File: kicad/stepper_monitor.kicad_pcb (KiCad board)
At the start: 2 copper layers, 38.5 x 43 mm, 54 parts, among them J1 Conn_01x04_Male, J2 Conn_01x04_Male, J3 Conn_01x02_Male, J4 USB_C_Receptacle_USB2.0, J5 JTAG, Q1 UMH3N, Q2 PJA3439, SW1 SW_Push, U1 CP2102N-A01-GQFN28, U2 AMS1117-3.3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

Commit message: Change adc filter caps from 4.7n to 2.2n
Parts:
- C17, C18: value 4n7 -> 2n2
- C7: value 4u7 -> 2u2
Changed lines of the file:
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@@
     (descr "Capacitor SMD 0402 (1005 Metric), square (rectangular) end terminal, IPC_7351 nominal, (Body size source: IPC-SM-782 page 76, https://www.pcb-3d.com/wordpress/wp-content/uploads/ipc-sm-782a_amendment_1_and_2.pdf), generated with kicad-footprint-generator")
     (tags "capacitor")
-    (property "LCSC" "C23733")
+    (property "LCSC" "C12530")
     (property "Sheetfile" "stepper_monitor.kicad_sch")
     (property "Sheetname" "")
@@
       (effects (font (size 1 1) (thickness 0.15)))
     )
-    (fp_text value "4u7" (at 0 1.16 90) (layer "F.Fab")
+    (fp_text value "2u2" (at 0 1.16 90) (layer "F.Fab")
       (effects (font (size 1 1) (thickness 0.15)))
     )
@@
     (descr "Capacitor SMD 0402 (1005 Metric), square (rectangular) end terminal, IPC_7351 nominal, (Body size source: IPC-SM-782 page 76, https://www.pcb-3d.com/wordpress/wp-content/uploads/ipc-sm-782a_amendment_1_and_2.pdf), generated with kicad-footprint-generator")
     (tags "capacitor")
-    (property "LCSC" "C1538")
+    (property "LCSC" "C1531")
     (property "Sheetfile" "stepper_monitor.kicad_sch")
     (property "Sheetname" "")
@@
       (effects (font (size 1 1) (thickness 0.15)))
     )
-    (fp_text value "4n7" (at 0 1.16) (layer "F.Fab")
+    (fp_text value "2n2" (at 0 1.16) (layer "F.Fab")
       (effects (font (size 1 1) (thickness 0.15)))
     )
@@
     (descr "Capacitor SMD 0402 (1005 Metric), square (rectangular) end terminal, IPC_7351 nominal, (Body size source: IPC-SM-782 page 76, https://www.pcb-3d.com/wordpress/wp-content/uploads/ipc-sm-782a_amendment_1_and_2.pdf), generated with kicad-footprint-generator")
     (tags "capacitor")
-    (property "LCSC" "C1538")
+    (property "LCSC" "C1531")
     (property "Sheetfile" "stepper_monitor.kicad_sch")
     (property "Sheetname" "")
@@
       (effects (font (size 1 1) (thickness 0.15)))
     )
-    (fp_text value "4n7" (at 0 1.16) (layer "F.Fab")
-      (effects (font (size 1 1) (thickness 0.15)))
-    )
+    (fp_text value "2n2" (at 0 1.16) (layer "F.Fab")
+      (effects (font (size 1 1) (thickness 0.15)))
+    )

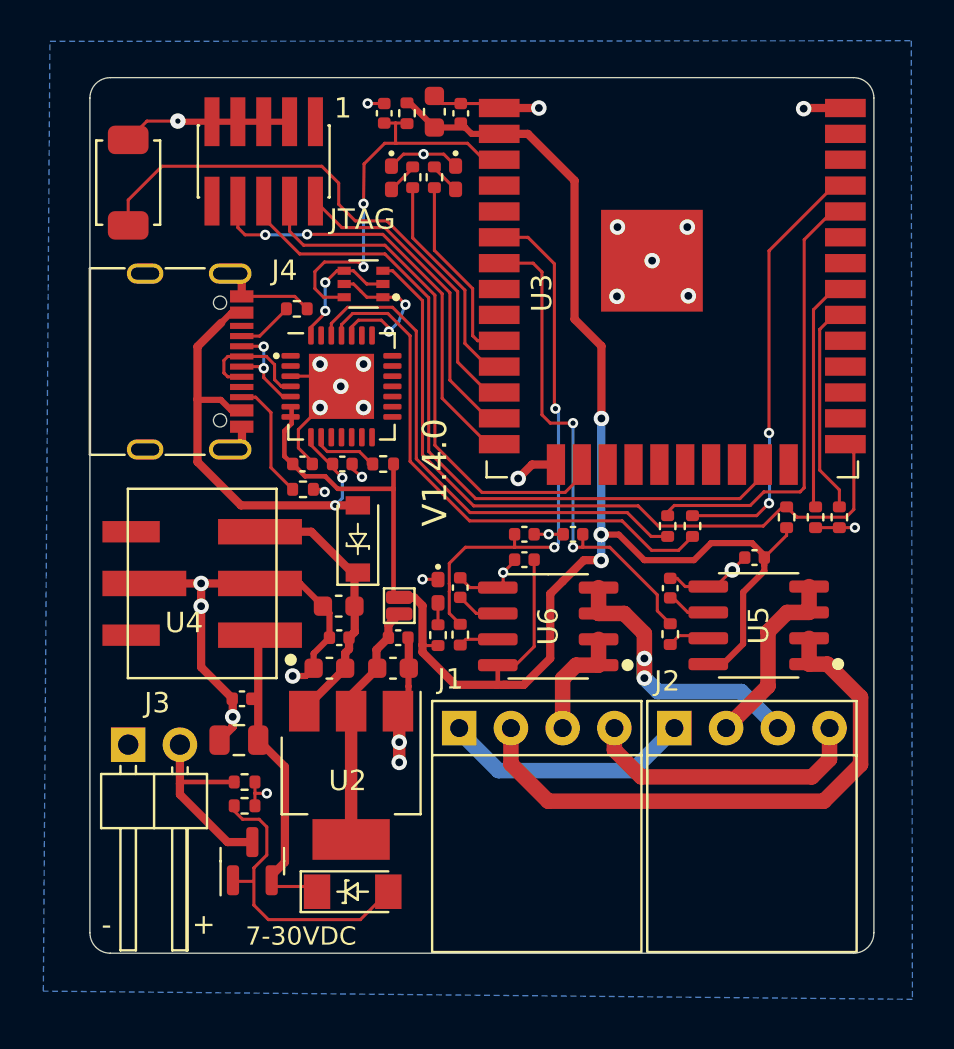
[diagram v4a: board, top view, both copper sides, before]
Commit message: Updated led and npn to available parts.
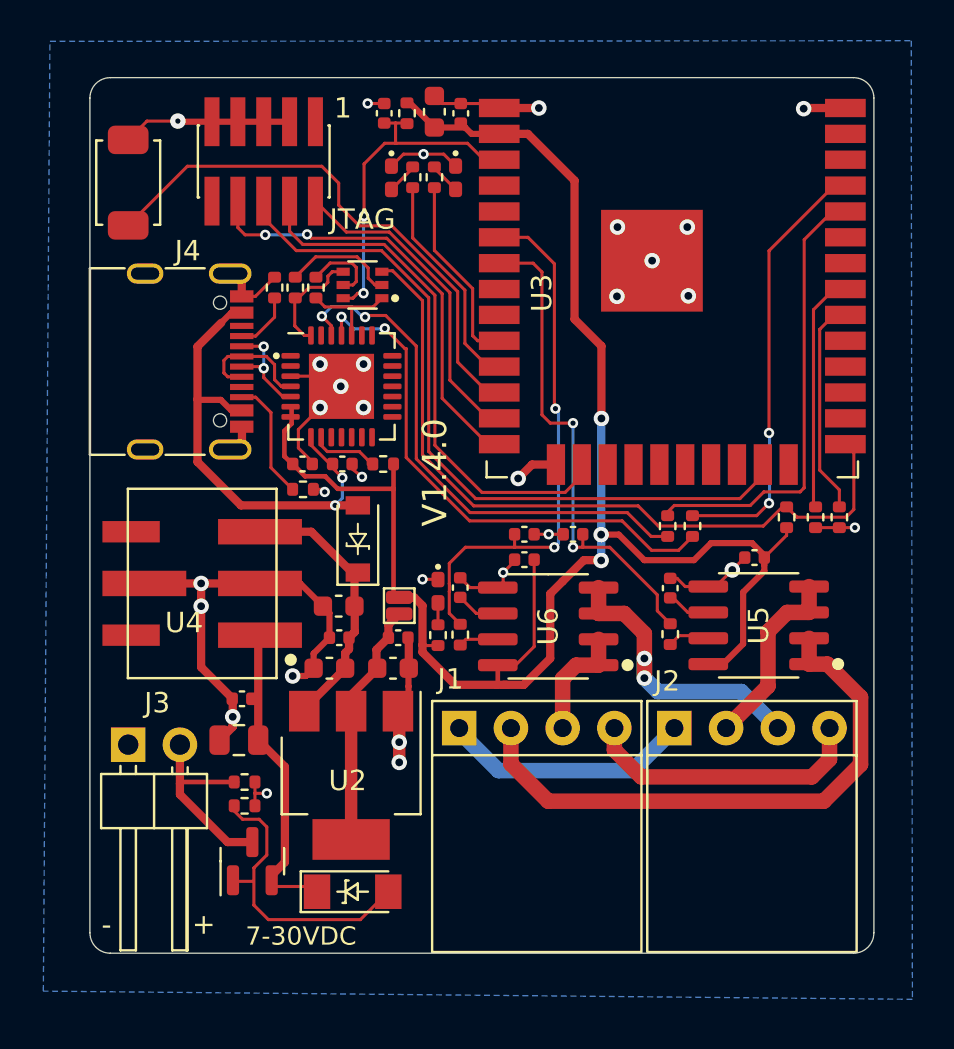
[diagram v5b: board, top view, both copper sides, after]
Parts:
- added R11: 5K1, Resistor_SMD:R_0402_1005Metric, F.Cu at (10.1, -32.7)
- added R18: 5K1, Resistor_SMD:R_0402_1005Metric, F.Cu at (11.1, -32.7)
- Q1: value UMH3N -> MMDT2222A
- moved R1 1.51 mm to (9.07, -32.7), turned to -90 degrees
- moved Q1 0.07 mm to (13.4, -32.8)
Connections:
- Q1 pad 2: DTR -> Net-(Q1-Pad2)
- Q1 pad 5: RTS -> Net-(Q1-Pad5)
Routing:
- net Net-(Q1-Pad2): track 0.00 -> 5.53 mm
- net Net-(Q1-Pad5): track 0.00 -> 3.77 mm
- net RTS: track 7.75 -> 4.98 mm, vias 2 -> 0
- net EN: track 20.5 -> 17.8 mm
- net DTR: track 6.23 -> 5.43 mm, vias 2 -> 0
- net SWITCH: track 27.4 -> 26.7 mm
- net Net-(R9-Pad2): track 25.8 -> 26.3 mm, vias 0 -> 2
- net Net-(R8-Pad2): track 26.7 -> 26.3 mm, vias 0 -> 2

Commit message: Updated PCB for external antenna + cleanups.
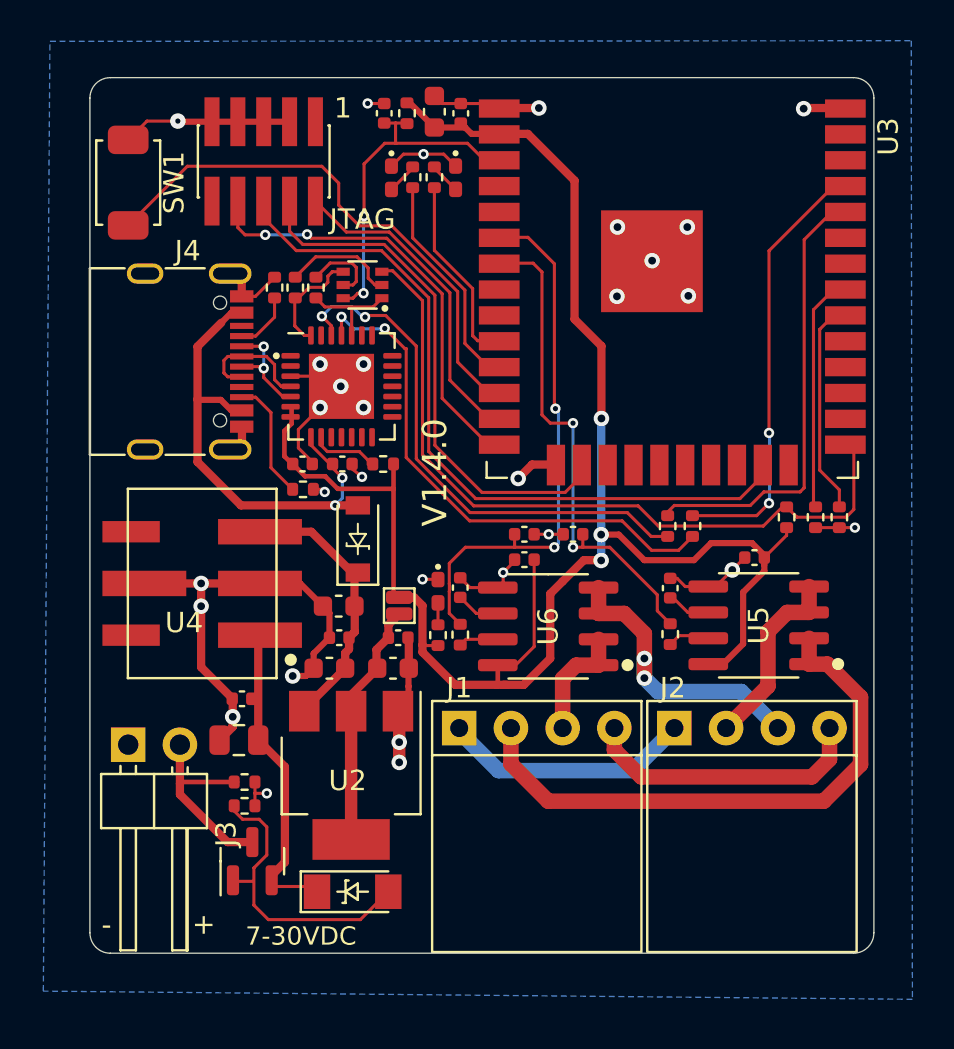
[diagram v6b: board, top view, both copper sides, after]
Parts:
- D1, D2, D3: footprint stepper_probe:LED_0402_1005Metric_Pad0.77x0.64mm_HandSolder -> stepper_monitor:LED_0402_1005Metric_Pad0.77x0.64mm_HandSolder
- J1, J2: footprint stepper_probe:connector_4pins_horizontal -> stepper_monitor:connector_4pins_horizontal
- J3: footprint stepper_probe:PinHeader_1x02_P2.54mm_Horizontal_JLCPCB -> stepper_monitor:PinHeader_1x02_P2.54mm_Horizontal_JLCPCB
- SW1: footprint stepper_probe:SW_Push_SPST_NO_Alps_SKRK -> stepper_monitor:SW_Push_SPST_NO_Alps_SKRK
- U3: value ESP32-WROOM-32 -> ESP32-WROOM-32U-N4; footprint stepper_monitor:ESP32-WROOM-32 -> stepper_monitor:ESP32-WROOM-32U
- moved U3 0.08 mm to (28.6, -32.4), turned to 90 degrees
- turned Q1 to 90 degrees
